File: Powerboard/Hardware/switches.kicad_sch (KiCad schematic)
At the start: 17 parts, among them J4 Conn_01x02_Male, J5 Conn_01x08_Male, J6 Conn_01x02_Male, Q1 PXP012-30QLJ, Q2 PXP012-30QLJ, Q3 PXP012-30QLJ, Q4 PXP012-30QLJ, U6 LTC4412xS6, U7 LTC4412xS6

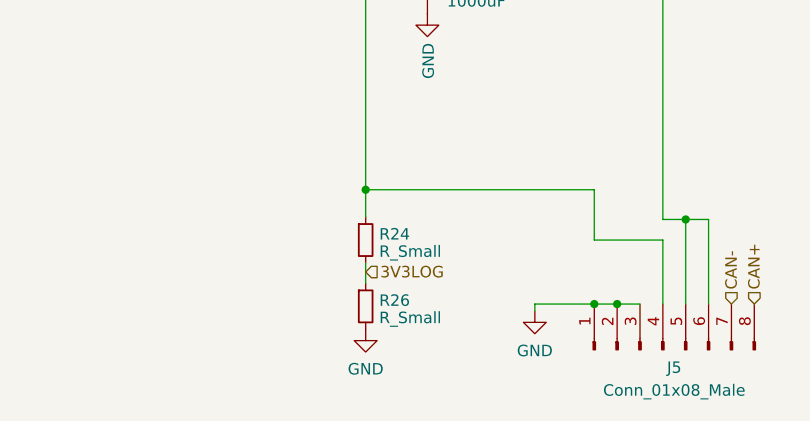
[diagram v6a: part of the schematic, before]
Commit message: 3v3logging moved to buck output
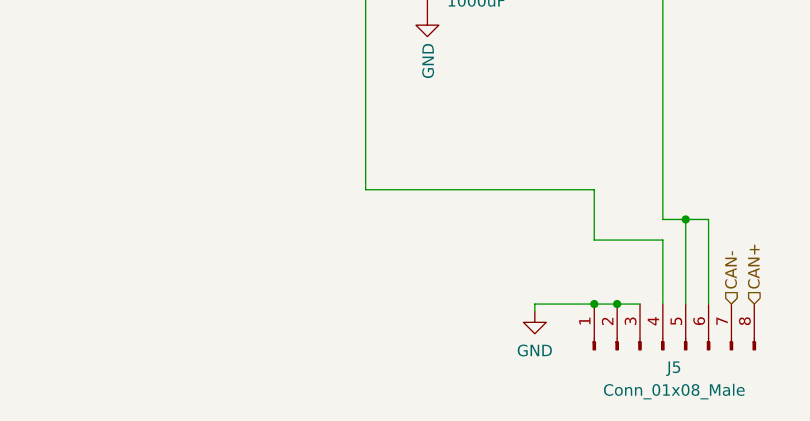
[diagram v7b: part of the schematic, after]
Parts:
- removed R24, R26: R_Small, Resistor_SMD:R_0402_1005Metric, symbol Device:R_Small
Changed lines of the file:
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@@
   (junction (at 104.902 111.506) (diameter 0) (color 0 0 0 0)
-  )
-  (junction (at 104.902 142.748) (diameter 0) (color 0 0 0 0)
   )
   (junction (at 104.902 56.388) (diameter 0) (color 0 0 0 0)
@@
     (stroke (width 0) (type default))
   )
-  (wire (pts (xy 104.902 150.876) (xy 104.902 153.162))
-    (stroke (width 0) (type default))
-  )
   (wire (pts (xy 145.8214 83.82) (xy 148.59 83.82))
     (stroke (width 0) (type default))
@@
   )
   (wire (pts (xy 167.894 99.822) (xy 171.704 99.822))
-    (stroke (width 0) (type default))
-  )
-  (wire (pts (xy 104.902 142.748) (xy 104.902 145.796))
     (stroke (width 0) (type default))
   )
@@
   )
   (hierarchical_label "3V3_SWITCH" (shape input) (at 70.612 68.072 90) (fields_autoplaced)
-    (effects (font (size 1.27 1.27)) (justify left))
-  )
-  (hierarchical_label "3V3LOG" (shape input) (at 104.902 151.892 0) (fields_autoplaced)
     (effects (font (size 1.27 1.27)) (justify left))
   )
@@
     )
   )
-  (symbol (lib_id "Device:R_Small") (at 104.902 155.702 0) (unit 1)
-    (in_bom yes) (on_board yes) (dnp no) (fields_autoplaced)
-    (property "Reference" "R26" (at 106.4006 155.0583 0)
-      (effects (font (size 1.27 1.27)) (justify left))
-    )
-    (property "Value" "R_Small" (at 106.4006 156.9793 0)
-      (effects (font (size 1.27 1.27)) (justify left))
-    )
-    (property "Footprint" "Resistor_SMD:R_0402_1005Metric" (at 104.902 155.702 0)
-      (effects (font (size 1.27 1.27)) hide)
-    )
-    (property "Datasheet" "~" (at 104.902 155.702 0)
-      (effects (font (size 1.27 1.27)) hide)
-    )
-    (pin "1")
-    (pin "2")
-    (instances
-      (project "Switcher"
-        (path "/e63e39d7-6ac0-4ffd-8aa3-1841a4541b55/133f56f4-a29c-4cbf-87b7-9d99a292e3c0"
-          (reference "R26") (unit 1)
-        )
-      )
-    )
-  )
   (symbol (lib_id "Jumper:SolderJumper_2_Bridged") (at 155.194 70.866 90) (unit 1)
     (in_bom yes) (on_board yes) (dnp no) (fields_autoplaced)
@@
         )
       )
-    )
-  )
-  (symbol (lib_id "power:GND") (at 104.902 158.242 0) (unit 1)
-    (in_bom yes) (on_board yes) (dnp no) (fields_autoplaced)
-    (property "Reference" "#PWR01" (at 104.902 164.592 0)
-      (effects (font (size 1.27 1.27)) hide)
-    )
-    (property "Value" "GND" (at 104.902 162.6854 0)
-      (effects (font (size 1.27 1.27)))
-    )
-    (property "Footprint" "" (at 104.902 158.242 0)
-      (effects (font (size 1.27 1.27)) hide)
-    )
-    (property "Datasheet" "" (at 104.902 158.242 0)
-      (effects (font (size 1.27 1.27)) hide)
-    )
-    (pin "1")
-    (instances
-      (project "Switcher"
-        (path "/e63e39d7-6ac0-4ffd-8aa3-1841a4541b55/133f56f4-a29c-4cbf-87b7-9d99a292e3c0"
-          (reference "#PWR01") (unit 1)
-        )
-      )
-    )
-  )
-  (symbol (lib_id "Device:R_Small") (at 104.902 148.336 0) (unit 1)
-    (in_bom yes) (on_board yes) (dnp no) (fields_autoplaced)
-    (property "Reference" "R24" (at 106.4006 147.6923 0)
-      (effects (font (size 1.27 1.27)) (justify left))
-    )
-    (property "Value" "R_Small" (at 106.4006 149.6133 0)
-      (effects (font (size 1.27 1.27)) (justify left))
-    )
-    (property "Footprint" "Resistor_SMD:R_0402_1005Metric" (at 104.902 148.336 0)
-      (effects (font (size 1.27 1.27)) hide)
-    )
-    (property "Datasheet" "~" (at 104.902 148.336 0)
-      (effects (font (size 1.27 1.27)) hide)
-    )
-    (pin "1")
-    (pin "2")
-    (instances
-      (project "Switcher"
-        (path "/e63e39d7-6ac0-4ffd-8aa3-1841a4541b55/133f56f4-a29c-4cbf-87b7-9d99a292e3c0"
-          (reference "R24") (unit 1)
-        )
-      )

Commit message: added some commands, hardware fixes
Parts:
- added 12VLED1: DEP_LED, LED_SMD:LED_0402_1005Metric, symbol Device:LED_Small
- added 3V3LED1: LOGIC_LED, LED_SMD:LED_0402_1005Metric, symbol Device:LED_Small
- added R14: 47k, Resistor_SMD:R_0402_1005Metric, symbol Device:R_Small
- added R22: 10k, Resistor_SMD:R_0402_1005Metric, symbol Device:R_Small
- added R7: 470, Resistor_SMD:R_0402_1005Metric, symbol Device:R_Small
- added R9: 3k, Resistor_SMD:R_0402_1005Metric, symbol Device:R_Small
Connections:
- net GND: now also 12VLED1.1 (K), 3V3LED1.1 (K), R22.2
- net at C23.1, J5.4 (Pin_4), Q1.5 (D_1)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: now also R7.2
- net at C24.1, J5.5 (Pin_5), J5.6 (Pin_6)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: now also R14.1, R9.1
- net 12V_SWITCH renamed DEP_SWITCH
- net 3V3_SWITCH renamed LOGIC_SWITCH
- new net: 12VLED1.2 (A), R9.2
- new net: 3V3LED1.2 (A), R7.1
- new net DepVoltage: R14.2, R22.1
